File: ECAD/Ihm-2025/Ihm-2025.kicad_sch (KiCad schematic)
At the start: 15 parts, among them SW1 SW_SPDT, SW2 SW_SPDT, SW3 SW_SPDT, SW4 SW_SPDT

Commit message: New IHM
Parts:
- removed D3, D4, D5: WS2812B, LED_SMD:LED_WS2812B_PLCC4_5.0x5.0mm_P3.2mm, symbol LED:WS2812B
- removed H1: M3, MountingHole:MountingHole_3.2mm_M3_Pad_Via, symbol Mechanical:MountingHole_Pad
- removed SW1, SW3: SW_SPDT, footprints:SK-12D10 1P2T, symbol Switch:SW_SPDT
- added C2: 100n, Capacitor_SMD:C_1206_3216Metric, symbol Device:C_Small
- added H2: M3, MountingHole:MountingHole_3.2mm_M3_Pad_Via, symbol Mechanical:MountingHole_Pad
- added R1: R_Small, Resistor_SMD:R_1206_3216Metric_Pad1.30x1.75mm_HandSolder, symbol Device:R_Small
- added R2: 4.8k, Resistor_SMD:R_1206_3216Metric_Pad1.30x1.75mm_HandSolder, symbol Device:R_Small
- added SW1: SW_Push, PCM_Switch_Keyboard_Cherry_MX:SW_Cherry_MX_PCB_1.00u, symbol Switch:SW_Push
- added U1: ~, Package_TO_SOT_SMD:SOT-23W, symbol Sensor_Magnetic:A1101ELHL
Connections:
- net +3V3: now also C2.1, R2.2, U1.1 (VCC)
- net GND: now also C2.2, H2.1, SW1.2, U1.3 (GND)
- net NEO_PIXEL: now also R1.1; no longer D1.4 (DIN)
- net DAC0 renamed Analog0
- net DAC1 renamed Analog1
- net Detection renamed Tirette
- net Tirette: now also R2.1, U1.2 (VOUT)
- net IHM_3 renamed Init
- net Init: now also SW1.1
- new net: D1.4 (DIN), R1.2
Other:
- moved on the sheet: C1, RV1, SW2, SW4

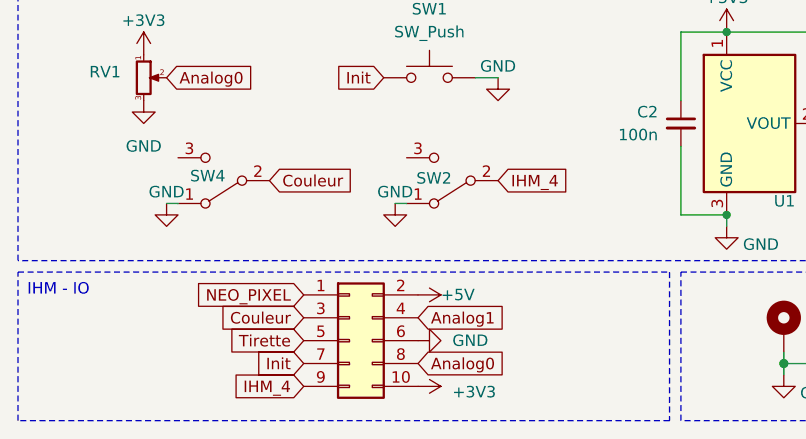
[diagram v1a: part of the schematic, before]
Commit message: WIP - comatibility 3.x 4.x
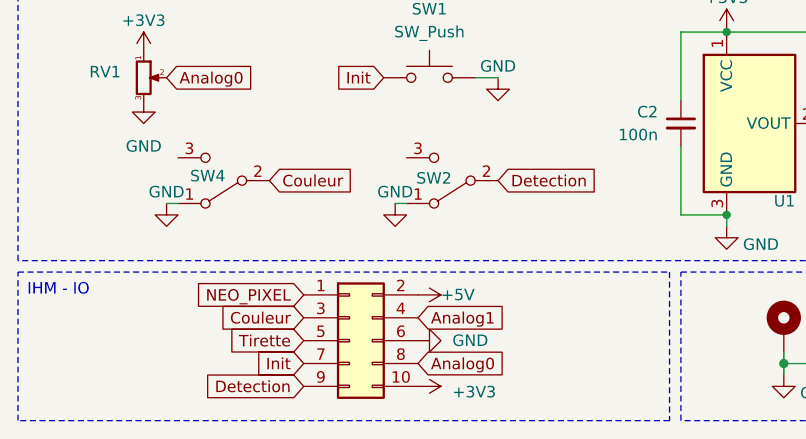
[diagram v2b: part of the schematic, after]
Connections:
- net IHM_4 renamed Detection
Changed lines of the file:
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@@
 		)
 	)
-	(global_label "IHM_4"
+	(global_label "Detection"
 		(shape input)
 		(at 143.51 110.49 0)
@@
 		)
 		(property "Intersheetrefs" "${INTERSHEET_REFS}"
-			(at 151.9796 110.49 0)
+			(at 155.3852 110.49 0)
 			(effects
 				(font
@@
 		)
 	)
-	(global_label "IHM_4"
+	(global_label "Detection"
 		(shape input)
 		(at 121.92 133.35 180)
@@
 		)
 		(property "Intersheetrefs" "${INTERSHEET_REFS}"
-			(at 113.3553 133.35 0)
+			(at 110.0448 133.35 0)
 			(effects
 				(font

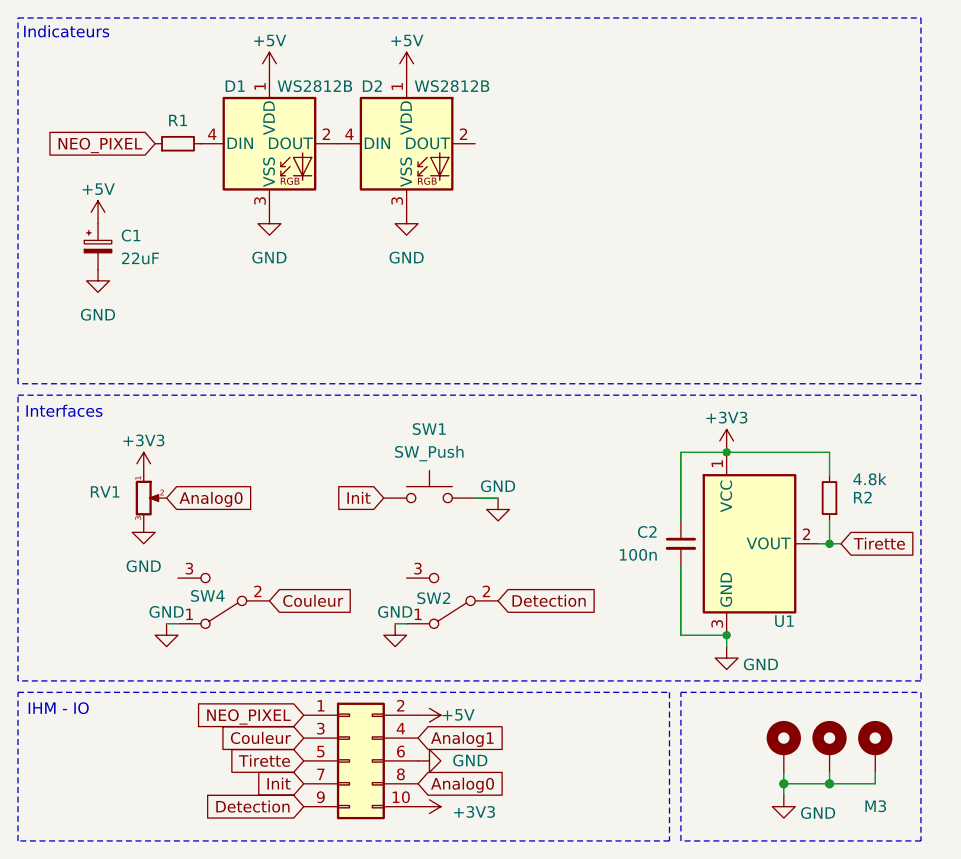
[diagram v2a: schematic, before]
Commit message: New halle effect sensor for tirette
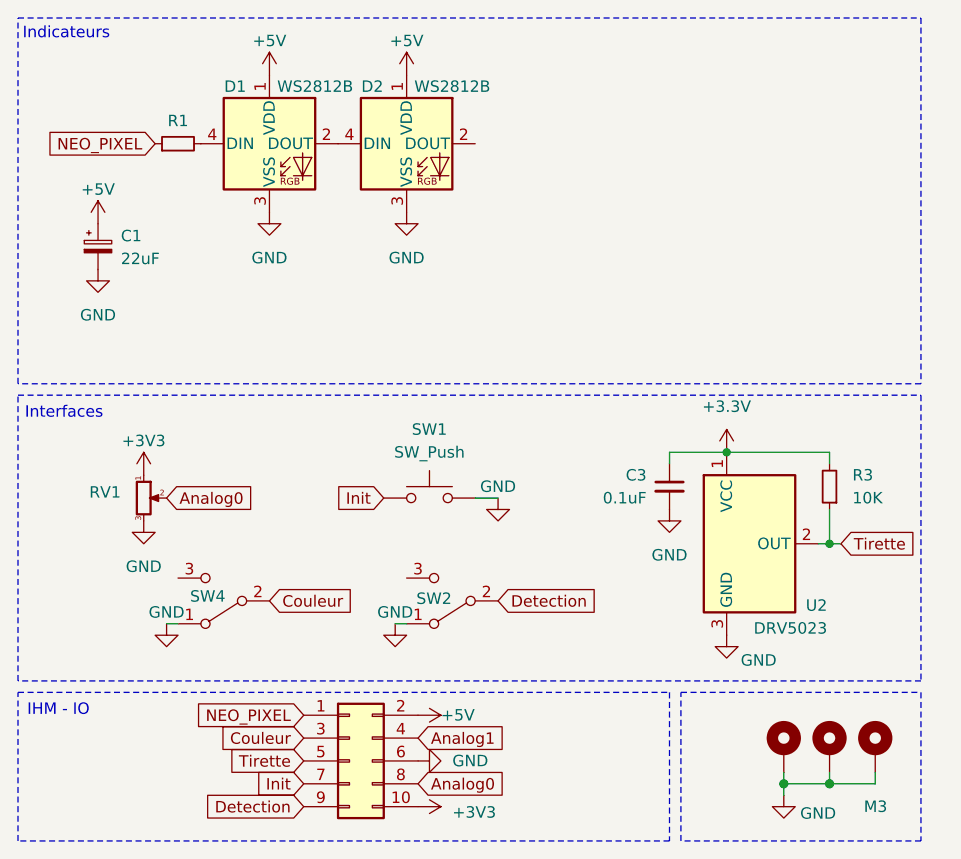
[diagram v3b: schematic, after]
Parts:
- removed C2: 100n, Capacitor_SMD:C_1206_3216Metric, symbol Device:C_Small
- removed R2: 4.8k, Resistor_SMD:R_1206_3216Metric_Pad1.30x1.75mm_HandSolder, symbol Device:R_Small
- removed U1: ~, Package_TO_SOT_SMD:SOT-23W, symbol Sensor_Magnetic:A1101ELHL
- added C3: 0.1uF, Capacitor_SMD:C_1206_3216Metric_Pad1.33x1.80mm_HandSolder, symbol Device:C_Small
- added R3: 10K, Resistor_SMD:R_1206_3216Metric_Pad1.30x1.75mm_HandSolder, symbol Device:R_Small
- added U2: DRV5023, Package_TO_SOT_SMD:SOT-23_Handsoldering, symbol Sensor_Magnetic:DRV5033AJxDBZ
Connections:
- net GND: now also C3.2, U2.3 (GND)
- net Tirette: now also R3.1, U2.2 (OUT)
- new net +3.3V: C3.1, R3.2, U2.1 (VCC)

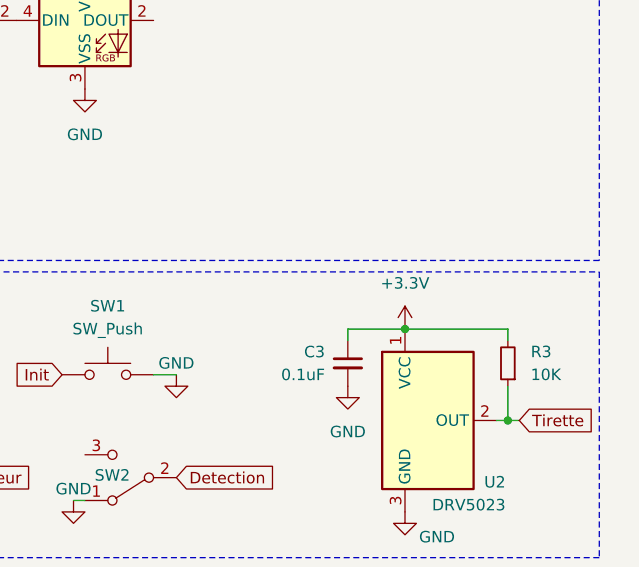
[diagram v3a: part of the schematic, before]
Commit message: fix 3.3V not connected to tirette
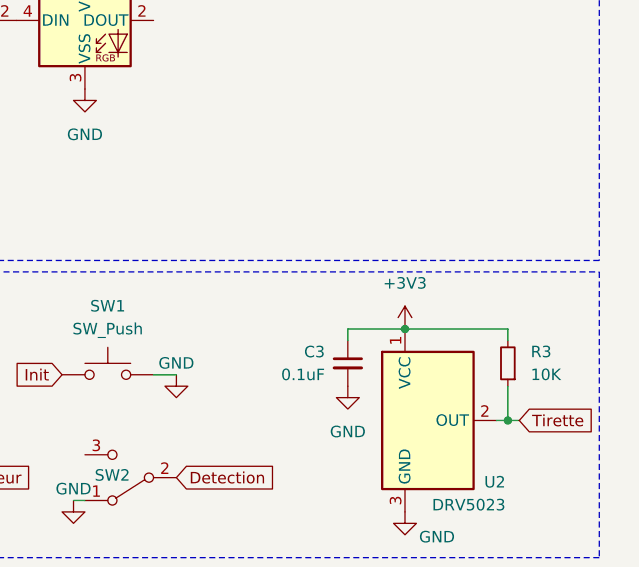
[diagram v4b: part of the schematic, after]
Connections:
- net +3.3V is gone; now on net +3V3: C3.1, R3.2, U2.1 (VCC)
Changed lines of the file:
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@@
-	)
-	(symbol
-		(lib_id "power:+3.3V")
-		(at 168.91 93.98 0)
-		(unit 1)
-		(exclude_from_sim no)
-		(in_bom yes)
-		(on_board yes)
-		(dnp no)
-		(fields_autoplaced yes)
-		(property "Reference" "#PWR06"
-			(at 168.91 97.79 0)
-			(effects
-				(font
-					(size 1.27 1.27)
-				)
-				(hide yes)
-			)
-		)
-		(property "Value" "+3.3V"
-			(at 168.91 88.9 0)
-			(effects
-				(font
-					(size 1.27 1.27)
-				)
-			)
-		)
-		(property "Footprint" ""
-			(at 168.91 93.98 0)
-			(effects
-				(font
-					(size 1.27 1.27)
-				)
-				(hide yes)
-			)
-		)
-		(property "Datasheet" ""
-			(at 168.91 93.98 0)
-			(effects
-				(font
-					(size 1.27 1.27)
-				)
-				(hide yes)
-			)
-		)
-		(property "Description" ""
-			(at 168.91 93.98 0)
-			(effects
-				(font
-					(size 1.27 1.27)
-				)
-				(hide yes)
-			)
-		)
-		(pin "1"
-		)
-		(instances
-			(project "Ihm-2025"
-				(path "/0aa37938-06b6-4526-91cd-cb876ed2e30a"
-					(reference "#PWR06")
-					(unit 1)
-				)
-			)
-		)
 	)
 	(symbol
@@
 					(unit 1)
 				)
+			)
+		)
+	)
+	(symbol
+		(lib_id "power:+3V3")
+		(at 168.91 93.98 0)
+		(unit 1)
+		(exclude_from_sim no)
+		(in_bom yes)
+		(on_board yes)
+		(dnp no)
+		(fields_autoplaced yes)
+		(property "Reference" "#PWR02"
+			(at 168.91 97.79 0)
+			(effects
+				(font
+					(size 1.27 1.27)
+				)
+				(hide yes)
+			)
+		)
+		(property "Value" "+3V3"
+			(at 168.91 88.9 0)
+			(effects
+				(font
+					(size 1.27 1.27)
+				)
+			)
+		)
+		(property "Footprint" ""
+			(at 168.91 93.98 0)
+			(effects
+				(font
+					(size 1.27 1.27)
+				)
+				(hide yes)
+			)
+		)
+		(property "Datasheet" ""
+			(at 168.91 93.98 0)
+			(effects
+				(font
+					(size 1.27 1.27)
+				)
+				(hide yes)
+			)
+		)
+		(property "Description" ""
+			(at 168.91 93.98 0)
+			(effects
+				(font
+					(size 1.27 1.27)
+				)
+				(hide yes)
+			)
+		)
+		(pin "1"
+		)
+		(instances
+			(project "Ihm-2025"
+				(path "/0aa37938-06b6-4526-91cd-cb876ed2e30a"
+					(reference "#PWR02")
+					(unit 1)
+				)
